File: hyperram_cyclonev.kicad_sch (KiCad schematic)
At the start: 64 parts, among them IC1 AP63205WU, IC2 TXB0108PWR, IC3 S26KL128SDABHI020, IC4 W25Q32JVSSIQ_TR, IC5 S27KL0641DABHI020, J1 ASP-122952-01, J2 HDMI_A, J3 Conn_02x10_Odd_Even, J4 Conn_02x06_Odd_Even, J5 Conn_02x06_Top_Bottom, J6 Conn_02x06_Top_Bottom, J7 Conn_02x06_Top_Bottom, Q1 BSS138, Q2 BSS138

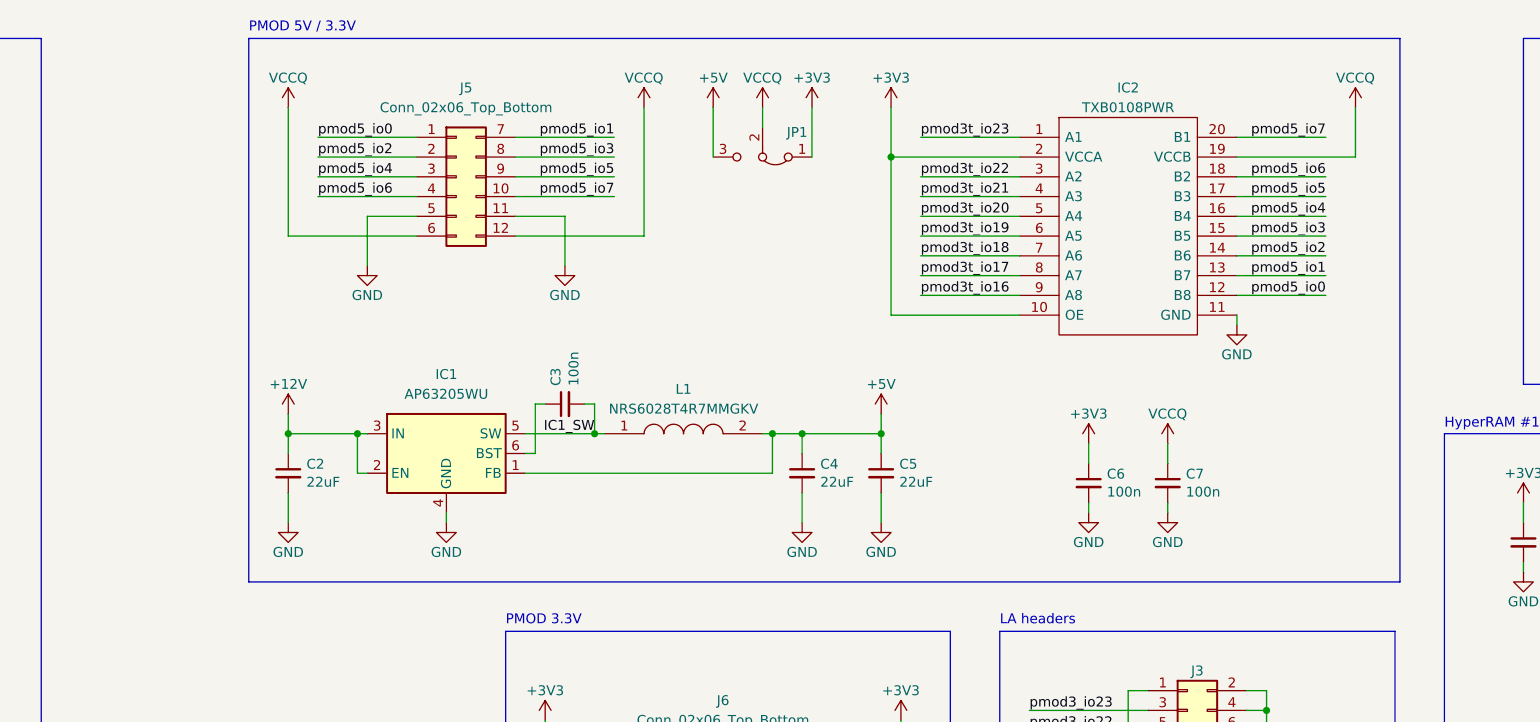
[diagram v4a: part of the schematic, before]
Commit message: Added second filtering input capacitor for DC/DC converter
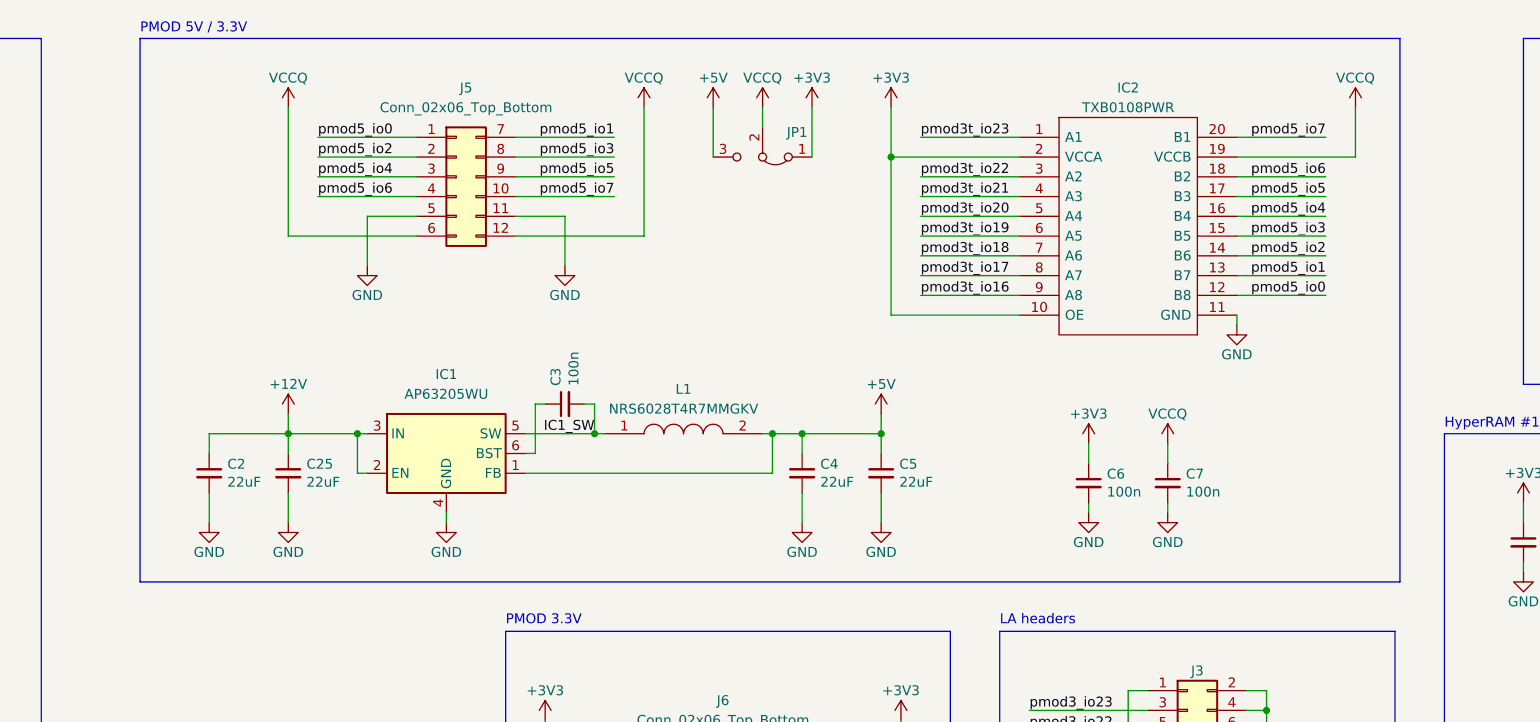
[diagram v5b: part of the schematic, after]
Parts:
- added C25: 22uF, Capacitor_SMD:C_0805_2012Metric_Pad1.18x1.45mm_HandSolder, symbol Device:C_Small
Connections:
- net +12V: now also C25.1
- net GND: now also C25.2
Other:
- moved on the sheet: C2
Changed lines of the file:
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@@
 	(wire
 		(pts
+			(xy 161.29 77.47) (xy 161.29 81.28)
+		)
+		(stroke
+			(width 0)
+			(type default)
+		)
+	)
+	(wire
+		(pts
 			(xy 86.36 118.11) (xy 99.06 118.11)
 		)
@@
 	(polyline
 		(pts
-			(xy 166.37 19.05) (xy 314.325 19.05)
+			(xy 152.4 19.05) (xy 314.325 19.05)
 		)
 		(stroke
@@
 	(wire
 		(pts
+			(xy 161.29 72.39) (xy 161.29 69.85)
+		)
+		(stroke
+			(width 0)
+			(type default)
+		)
+	)
+	(wire
+		(pts
 			(xy 158.75 215.9) (xy 172.72 215.9)
 		)
@@
 	(wire
 		(pts
+			(xy 161.29 69.85) (xy 171.45 69.85)
+		)
+		(stroke
+			(width 0)
+			(type default)
+		)
+	)
+	(wire
+		(pts
 			(xy 384.81 229.87) (xy 383.54 229.87)
 		)
@@
 	(polyline
 		(pts
-			(xy 166.37 19.05) (xy 166.37 88.9)
+			(xy 152.4 19.05) (xy 152.4 88.9)
 		)
 		(stroke
@@
 	(polyline
 		(pts
-			(xy 314.325 88.9) (xy 166.37 88.9)
+			(xy 314.325 88.9) (xy 152.4 88.9)
 		)
 		(stroke
@@
 	(text "PMOD 5V / 3.3V"
 		(exclude_from_sim no)
-		(at 166.37 18.415 0)
+		(at 152.4 18.542 0)
 		(effects
 			(font
@@
 	(symbol
 		(lib_id "Device:C_Small")
-		(at 171.45 74.93 0)
+		(at 161.29 74.93 0)
 		(unit 1)
 		(exclude_from_sim no)
@@
 		(dnp no)
 		(property "Reference" "C2"
-			(at 173.7868 73.7616 0)
+			(at 163.6268 73.7616 0)
 			(effects
 				(font
@@
 		)
 		(property "Value" "22uF"
-			(at 173.7868 76.073 0)
+			(at 163.6268 76.073 0)
 			(effects
 				(font
@@
 		)
 		(property "Footprint" "Capacitor_SMD:C_0805_2012Metric_Pad1.18x1.45mm_HandSolder"
-			(at 171.45 74.93 0)
+			(at 161.29 74.93 0)
 			(effects
 				(font
@@
 		)
 		(property "Datasheet" "~"
-			(at 171.45 74.93 0)
+			(at 161.29 74.93 0)
 			(effects
 				(font
@@
 		)
 		(property "Description" ""
-			(at 171.45 74.93 0)
+			(at 161.29 74.93 0)
 			(effects
 				(font
@@
 		)
 		(property "Part" "CL21A226MAYNNNE "
-			(at 171.45 74.93 0)
+			(at 161.29 74.93 0)
 			(effects
 				(font
@@
 		(lib_name "GND_1")
 		(lib_id "power:GND")
+		(at 161.29 81.28 0)
+		(unit 1)
+		(exclude_from_sim no)
+		(in_bom yes)
+		(on_board yes)
+		(dnp no)
+		(property "Reference" "#PWR013"
+			(at 161.29 87.63 0)
+			(effects
+				(font
+					(size 1.27 1.27)
+				)
+				(hide yes)
+			)
+		)
+		(property "Value" "GND"
+			(at 161.29 85.09 0)
+			(effects
+				(font
+					(size 1.27 1.27)
+				)
+			)
+		)
+		(property "Footprint" ""
+			(at 161.29 81.28 0)
+			(effects
+				(font
+					(size 1.27 1.27)
+				)
+				(hide yes)
+			)
+		)
+		(property "Datasheet" ""
+			(at 161.29 81.28 0)
+			(effects
+				(font
+					(size 1.27 1.27)
+				)
+				(hide yes)
+			)
+		)
+		(property "Description" "Power symbol creates a global label with name \"GND\" , ground"
+			(at 161.29 81.28 0)
+			(effects
+				(font
+					(size 1.27 1.27)
+				)
+				(hide yes)
+			)
+		)
+		(pin "1"
+		)
+		(instances
+			(project "hyperram_cyclonev"
+				(path "/42eba7a3-1298-45f5-b9c6-7800ee22d64c"
+					(reference "#PWR013")
+					(unit 1)
+				)
+			)
+		)
+	)
+	(symbol
+		(lib_name "GND_1")
+		(lib_id "power:GND")
 		(at 63.5 273.05 0)
 		(unit 1)
@@
 					(unit 1)
 				)
+			)
+		)
+	)
+	(symbol
+		(lib_id "Device:C_Small")
+		(at 171.45 74.93 0)
+		(unit 1)
+		(exclude_from_sim no)
+		(in_bom yes)
+		(on_board yes)
+		(dnp no)
+		(property "Reference" "C25"
+			(at 173.7868 73.7616 0)
+			(effects
+				(font
+					(size 1.27 1.27)
+				)
+				(justify left)
+			)
+		)
+		(property "Value" "22uF"
+			(at 173.7868 76.073 0)
+			(effects
+				(font
+					(size 1.27 1.27)
+				)
+				(justify left)
+			)
+		)
+		(property "Footprint" "Capacitor_SMD:C_0805_2012Metric_Pad1.18x1.45mm_HandSolder"
+			(at 171.45 74.93 0)
+			(effects
+				(font
+					(size 1.27 1.27)
+				)
+				(hide yes)
+			)
+		)
+		(property "Datasheet" "~"
+			(at 171.45 74.93 0)
+			(effects
+				(font
+					(size 1.27 1.27)
+				)
+				(hide yes)
+			)
+		)
+		(property "Description" ""
+			(at 171.45 74.93 0)
+			(effects
+				(font
+					(size 1.27 1.27)
+				)
+				(hide yes)
+			)
+		)
+		(property "Part" "CL21A226MAYNNNE "
+			(at 171.45 74.93 0)
+			(effects
+				(font
+					(size 1.27 1.27)
+				)
+				(hide yes)
+			)
+		)
+		(pin "1"
+		)
+		(pin "2"
+		)
+		(instances
+			(project "hyperram_cyclonev"
+				(path "/42eba7a3-1298-45f5-b9c6-7800ee22d64c"
+					(reference "C25")
+					(unit 1)
+				)

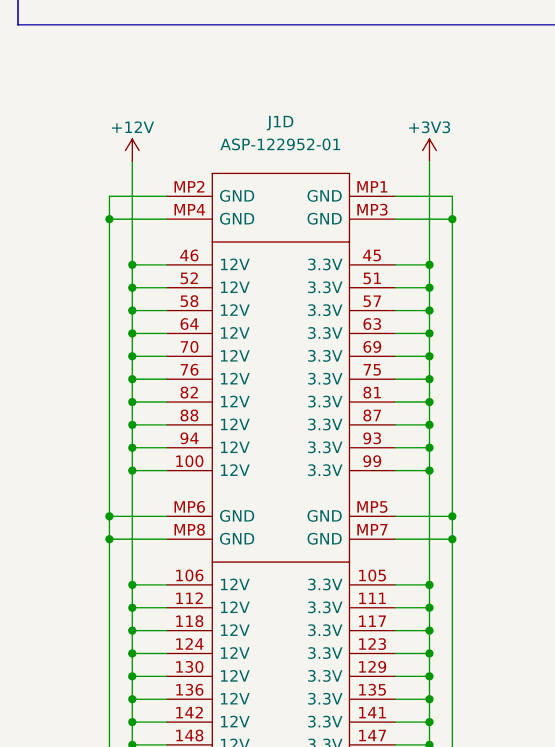
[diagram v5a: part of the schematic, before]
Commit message: Marked unused 12V pins as NC
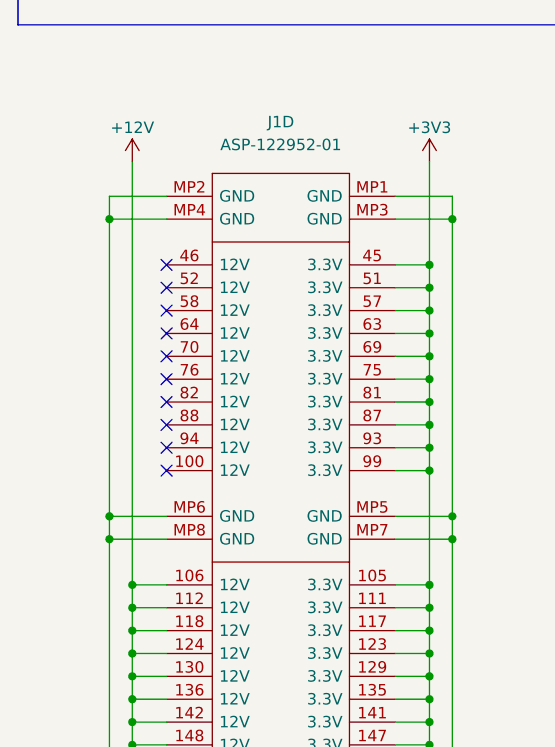
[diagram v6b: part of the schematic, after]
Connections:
- net +12V: no longer J1.100 (12V), J1.46 (12V), J1.52 (12V), J1.58 (12V), J1.64 (12V), J1.70 (12V), J1.76 (12V), J1.82 (12V), J1.88 (12V), J1.94 (12V)
- no-connect marks 8 -> 18
